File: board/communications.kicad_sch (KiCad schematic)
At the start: 6 parts, among them J1 RJ45_LED_Shielded, U3 ATA6561

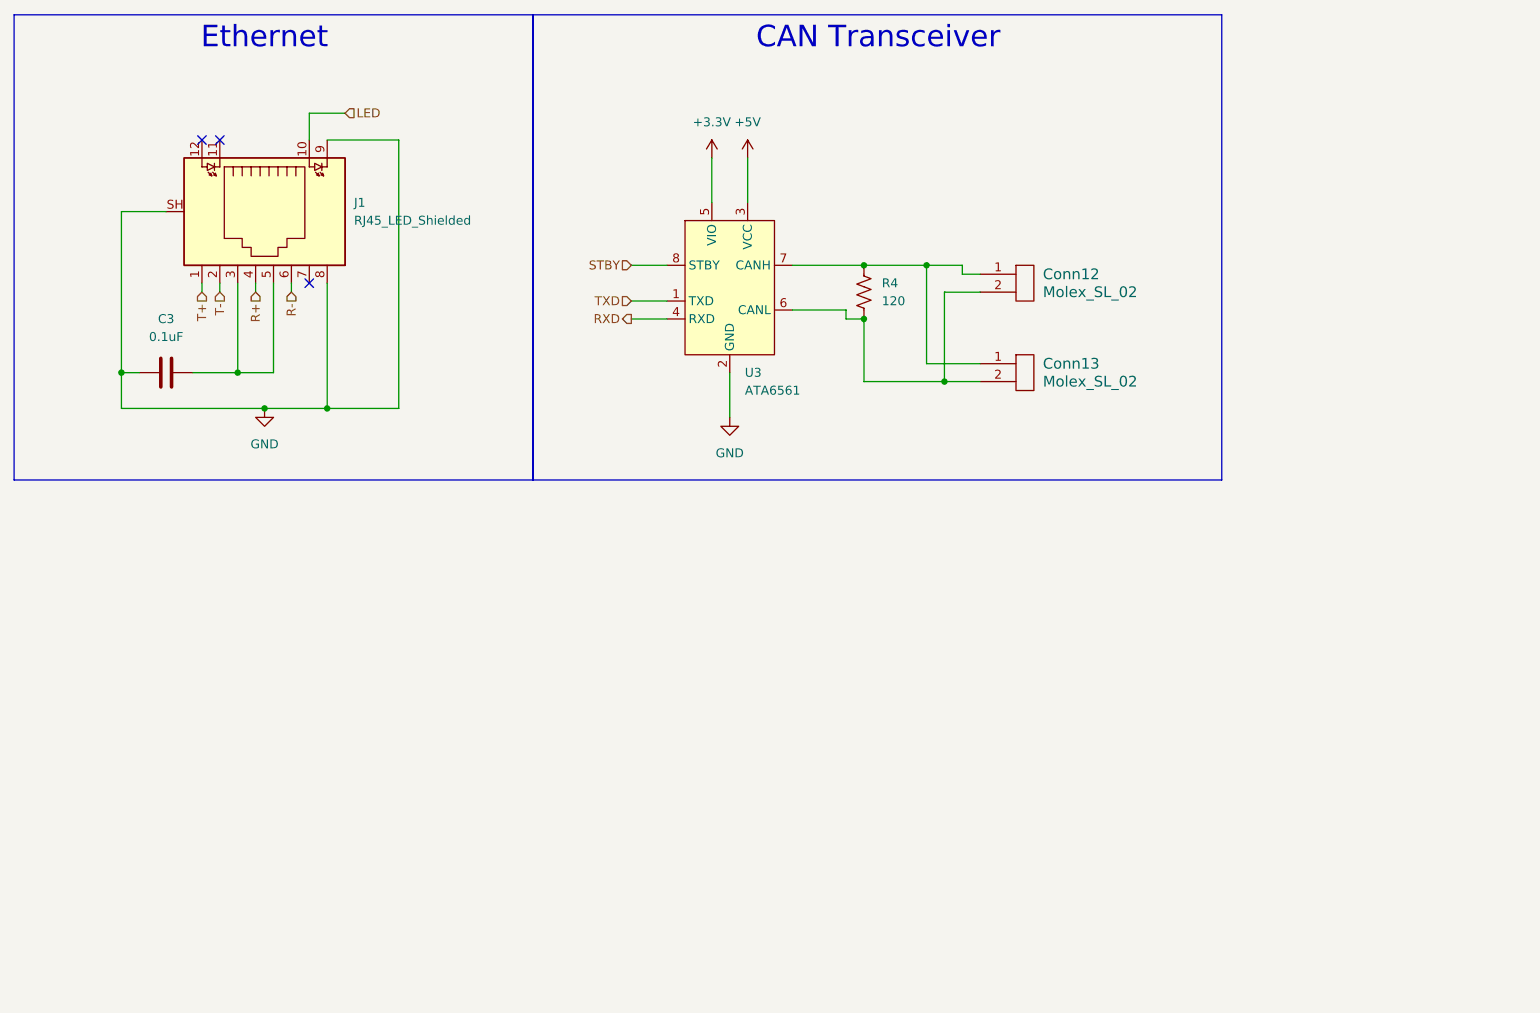
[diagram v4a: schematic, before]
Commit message: Added second CAN tranceiver and a switch
also imported a new symbol for both the switch symbol and its footprint
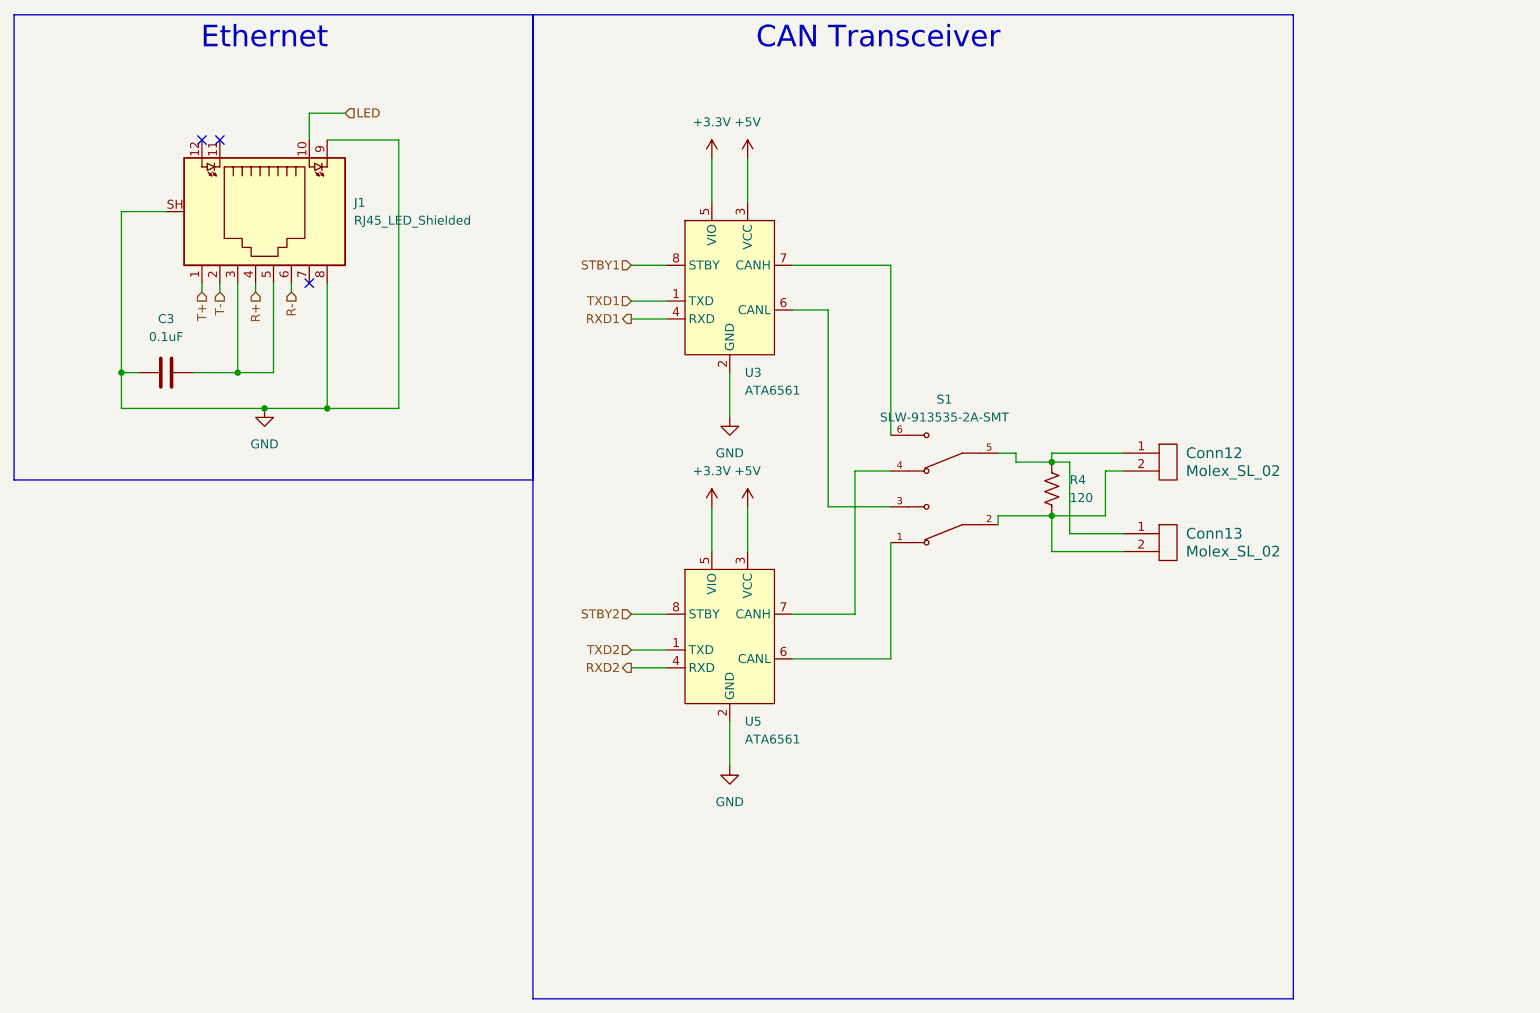
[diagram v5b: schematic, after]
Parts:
- added S1: SLW-913535-2A-SMT, MRDT_Switches:SW_SLW-913535-2A-SMT, symbol MRDT_Switches:SLW-913535-2A-SMT
- added U5: ATA6561, Package_SO:SOIC-8_3.9x4.9mm_P1.27mm, symbol MRDT_Devices:ATA6561
- R4: footprint Resistor_SMD:R_0603_1608Metric_Pad0.98x0.95mm_HandSolder -> (none)
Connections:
- net +3.3V: now also U5.5 (VIO)
- net +5V: now also U5.3 (VCC)
- net GND: now also U5.2 (GND)
- net at Conn12.1, Conn13.1, R4.1: now also S1.5; no longer U3.7 (CANH)
- net at Conn12.2, Conn13.2, R4.2: now also S1.2; no longer U3.6 (CANL)
- net RXD renamed RXD1
- net STBY renamed STBY1
- net TXD renamed TXD1
- new net: S1.1, U5.6 (CANL)
- new net: S1.4, U5.7 (CANH)
- new net: S1.3, U3.6 (CANL)
- new net: S1.6, U3.7 (CANH)
- new net RXD2: U5.4 (RXD)
- new net STBY2: U5.8 (STBY)
- new net TXD2: U5.1 (TXD)
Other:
- moved on the sheet: Conn12, Conn13

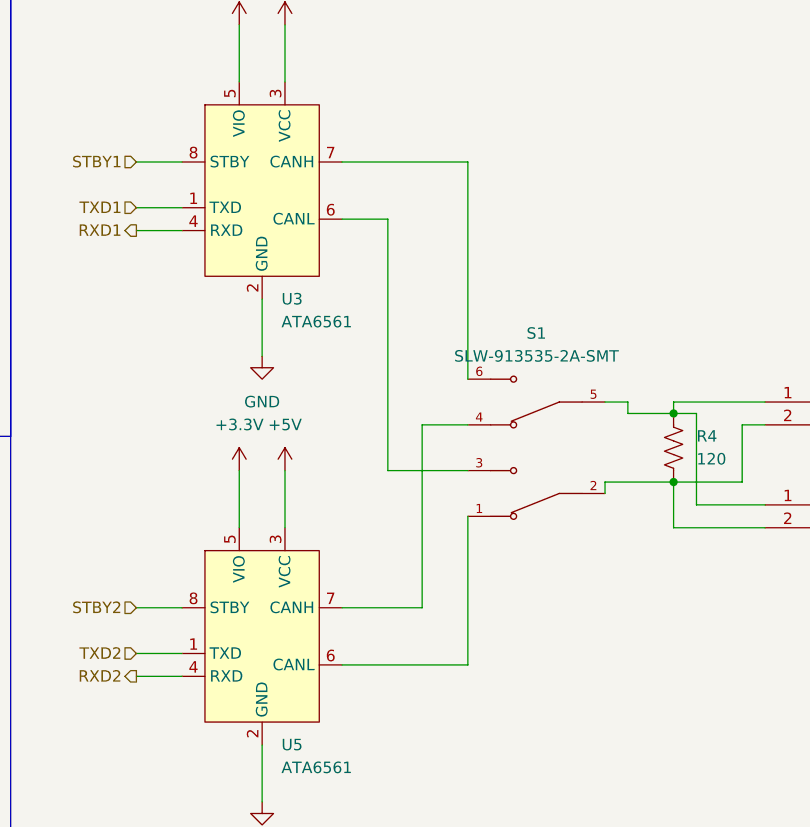
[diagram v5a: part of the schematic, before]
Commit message: Added Second CAN and Switch
Retraced CAN signal lines and added a second transceiver going to a switch
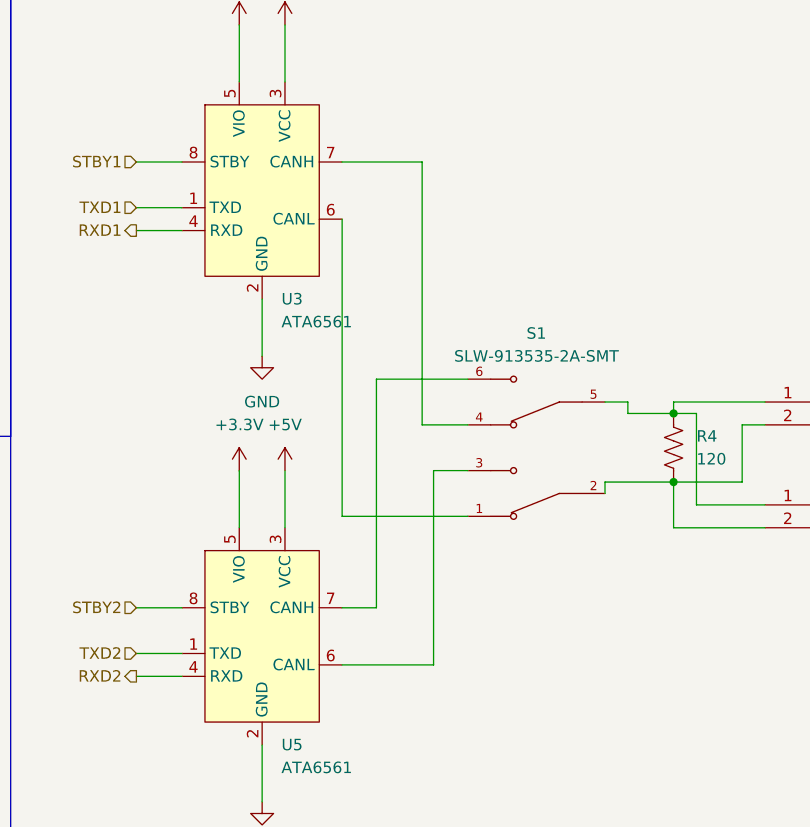
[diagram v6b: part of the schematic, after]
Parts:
- R4: footprint (none) -> Resistor_SMD:R_0603_1608Metric_Pad0.98x0.95mm_HandSolder
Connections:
- net at U5.6 (CANL): now also S1.3; no longer S1.1
- net at U5.7 (CANH): now also S1.6; no longer S1.4
- net at U3.6 (CANL): now also S1.1; no longer S1.3
- net at U3.7 (CANH): now also S1.4; no longer S1.6
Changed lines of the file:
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@@
-	(wire
-		(pts
-			(xy 123.19 104.14) (xy 137.16 104.14)
-		)
-		(stroke
-			(width 0)
-			(type default)
-		)
-	)
 	(wire
 		(pts
@@
 	(wire
 		(pts
+			(xy 127 72.39) (xy 127 97.79)
+		)
+		(stroke
+			(width 0)
+			(type default)
+		)
+	)
+	(wire
+		(pts
+			(xy 100.33 48.26) (xy 105.41 48.26)
+		)
+		(stroke
+			(width 0)
+			(type default)
+		)
+	)
+	(wire
+		(pts
+			(xy 114.3 63.5) (xy 114.3 69.85)
+		)
+		(stroke
+			(width 0)
+			(type default)
+		)
+	)
+	(wire
+		(pts
+			(xy 123.19 87.63) (xy 137.16 87.63)
+		)
+		(stroke
+			(width 0)
+			(type default)
+		)
+	)
+	(wire
+		(pts
+			(xy 160.02 76.2) (xy 162.56 76.2)
+		)
+		(stroke
+			(width 0)
+			(type default)
+		)
+	)
+	(wire
+		(pts
+			(xy 52.07 50.8) (xy 52.07 52.07)
+		)
+		(stroke
+			(width 0)
+			(type default)
+		)
+	)
+	(wire
+		(pts
+			(xy 160.02 74.93) (xy 170.18 74.93)
+		)
+		(stroke
+			(width 0)
+			(type default)
+		)
+	)
+	(wire
+		(pts
+			(xy 54.61 26.67) (xy 59.69 26.67)
+		)
+		(stroke
+			(width 0)
+			(type default)
+		)
+	)
+	(wire
+		(pts
+			(xy 123.19 54.61) (xy 123.19 87.63)
+		)
+		(stroke
+			(width 0)
+			(type default)
+		)
+	)
+	(wire
+		(pts
+			(xy 160.02 76.2) (xy 160.02 74.93)
+		)
+		(stroke
+			(width 0)
+			(type default)
+		)
+	)
+	(wire
+		(pts
+			(xy 152.4 83.82) (xy 152.4 85.09)
+		)
+		(stroke
+			(width 0)
+			(type default)
+		)
+	)
+	(wire
+		(pts
+			(xy 54.61 30.48) (xy 54.61 26.67)
+		)
+		(stroke
+			(width 0)
+			(type default)
+		)
+	)
+	(wire
+		(pts
+			(xy 162.56 86.36) (xy 170.18 86.36)
+		)
+		(stroke
+			(width 0)
+			(type default)
+		)
+	)
+	(wire
+		(pts
+			(xy 116.84 82.55) (xy 116.84 88.9)
+		)
+		(stroke
+			(width 0)
+			(type default)
+		)
+	)
+	(wire
+		(pts
+			(xy 100.33 105.41) (xy 105.41 105.41)
+		)
+		(stroke
+			(width 0)
+			(type default)
+		)
+	)
+	(wire
+		(pts
+			(xy 133.35 82.55) (xy 137.16 82.55)
+		)
+		(stroke
+			(width 0)
+			(type default)
+		)
+	)
+	(wire
+		(pts
+			(xy 160.02 83.82) (xy 160.02 88.9)
+		)
+		(stroke
+			(width 0)
+			(type default)
+		)
+	)
+	(wire
+		(pts
+			(xy 39.37 50.8) (xy 39.37 52.07)
+		)
+		(stroke
+			(width 0)
+			(type default)
+		)
+	)
+	(wire
+		(pts
 			(xy 132.08 77.47) (xy 137.16 77.47)
 		)
@@
 	(wire
 		(pts
-			(xy 132.08 97.79) (xy 132.08 77.47)
-		)
-		(stroke
-			(width 0)
-			(type default)
-		)
-	)
-	(wire
-		(pts
-			(xy 100.33 48.26) (xy 105.41 48.26)
-		)
-		(stroke
-			(width 0)
-			(type default)
-		)
-	)
-	(wire
-		(pts
-			(xy 137.16 48.26) (xy 137.16 72.39)
-		)
-		(stroke
-			(width 0)
-			(type default)
-		)
-	)
-	(wire
-		(pts
-			(xy 114.3 63.5) (xy 114.3 69.85)
-		)
-		(stroke
-			(width 0)
-			(type default)
-		)
-	)
-	(wire
-		(pts
-			(xy 160.02 76.2) (xy 162.56 76.2)
-		)
-		(stroke
-			(width 0)
-			(type default)
-		)
-	)
-	(wire
-		(pts
-			(xy 52.07 50.8) (xy 52.07 52.07)
-		)
-		(stroke
-			(width 0)
-			(type default)
-		)
-	)
-	(wire
-		(pts
-			(xy 160.02 74.93) (xy 170.18 74.93)
-		)
-		(stroke
-			(width 0)
-			(type default)
-		)
-	)
-	(wire
-		(pts
-			(xy 54.61 26.67) (xy 59.69 26.67)
-		)
-		(stroke
-			(width 0)
-			(type default)
-		)
-	)
-	(wire
-		(pts
-			(xy 160.02 76.2) (xy 160.02 74.93)
-		)
-		(stroke
-			(width 0)
-			(type default)
-		)
-	)
-	(wire
-		(pts
-			(xy 152.4 83.82) (xy 152.4 85.09)
-		)
-		(stroke
-			(width 0)
-			(type default)
-		)
-	)
-	(wire
-		(pts
-			(xy 54.61 30.48) (xy 54.61 26.67)
-		)
-		(stroke
-			(width 0)
-			(type default)
-		)
-	)
-	(wire
-		(pts
-			(xy 162.56 86.36) (xy 170.18 86.36)
-		)
-		(stroke
-			(width 0)
-			(type default)
-		)
-	)
-	(wire
-		(pts
-			(xy 116.84 82.55) (xy 116.84 88.9)
-		)
-		(stroke
-			(width 0)
-			(type default)
-		)
-	)
-	(wire
-		(pts
-			(xy 100.33 105.41) (xy 105.41 105.41)
-		)
-		(stroke
-			(width 0)
-			(type default)
-		)
-	)
-	(wire
-		(pts
-			(xy 160.02 83.82) (xy 160.02 88.9)
-		)
-		(stroke
-			(width 0)
-			(type default)
-		)
-	)
-	(wire
-		(pts
-			(xy 39.37 50.8) (xy 39.37 52.07)
-		)
-		(stroke
-			(width 0)
-			(type default)
-		)
-	)
-	(wire
-		(pts
 			(xy 100.33 102.87) (xy 105.41 102.87)
 		)
@@
 	(wire
 		(pts
+			(xy 123.19 48.26) (xy 132.08 48.26)
+		)
+		(stroke
+			(width 0)
+			(type default)
+		)
+	)
+	(wire
+		(pts
 			(xy 57.15 50.8) (xy 57.15 68.58)
 		)
@@
 	(wire
 		(pts
+			(xy 127 72.39) (xy 137.16 72.39)
+		)
+		(stroke
+			(width 0)
+			(type default)
+		)
+	)
+	(wire
+		(pts
+			(xy 133.35 104.14) (xy 133.35 82.55)
+		)
+		(stroke
+			(width 0)
+			(type default)
+		)
+	)
+	(wire
+		(pts
 			(xy 154.94 74.93) (xy 154.94 76.2)
 		)
@@
 	(wire
 		(pts
-			(xy 123.19 48.26) (xy 137.16 48.26)
-		)
-		(stroke
-			(width 0)
-			(type default)
-		)
-	)
-	(wire
-		(pts
 			(xy 167.64 77.47) (xy 170.18 77.47)
 		)
@@
 	(wire
 		(pts
-			(xy 128.27 82.55) (xy 137.16 82.55)
-		)
-		(stroke
-			(width 0)
-			(type default)
-		)
-	)
-	(wire
-		(pts
-			(xy 123.19 97.79) (xy 132.08 97.79)
+			(xy 123.19 97.79) (xy 127 97.79)
+		)
+		(stroke
+			(width 0)
+			(type default)
+		)
+	)
+	(wire
+		(pts
+			(xy 123.19 104.14) (xy 133.35 104.14)
 		)
 		(stroke
@@
 	(wire
 		(pts
-			(xy 123.19 54.61) (xy 128.27 54.61)
-		)
-		(stroke
-			(width 0)
-			(type default)
-		)
-	)
-	(wire
-		(pts
 			(xy 162.56 76.2) (xy 162.56 86.36)
 		)
@@
 	(wire
 		(pts
-			(xy 128.27 54.61) (xy 128.27 82.55)
-		)
-		(stroke
-			(width 0)
-			(type default)
-		)
-	)
-	(wire
-		(pts
 			(xy 152.4 74.93) (xy 154.94 74.93)
 		)
@@
 	(wire
 		(pts
-			(xy 137.16 104.14) (xy 137.16 87.63)
-		)
-		(stroke
-			(width 0)
-			(type default)
-		)
-	)
-	(wire
-		(pts
 			(xy 49.53 50.8) (xy 49.53 63.5)
 		)
@@
 		(pts
 			(xy 100.33 97.79) (xy 105.41 97.79)
+		)
+		(stroke
+			(width 0)
+			(type default)
+		)
+	)
+	(wire
+		(pts
+			(xy 132.08 48.26) (xy 132.08 77.47)
 		)
 		(stroke
@@
 			)
 		)
-		(property "Footprint" ""
+		(property "Footprint" "Resistor_SMD:R_0603_1608Metric_Pad0.98x0.95mm_HandSolder"
 			(at 161.036 80.264 90)
 			(effects
